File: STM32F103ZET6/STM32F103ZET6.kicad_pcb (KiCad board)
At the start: 2 copper layers, 1 part, among them U1 STM32F103ZETx

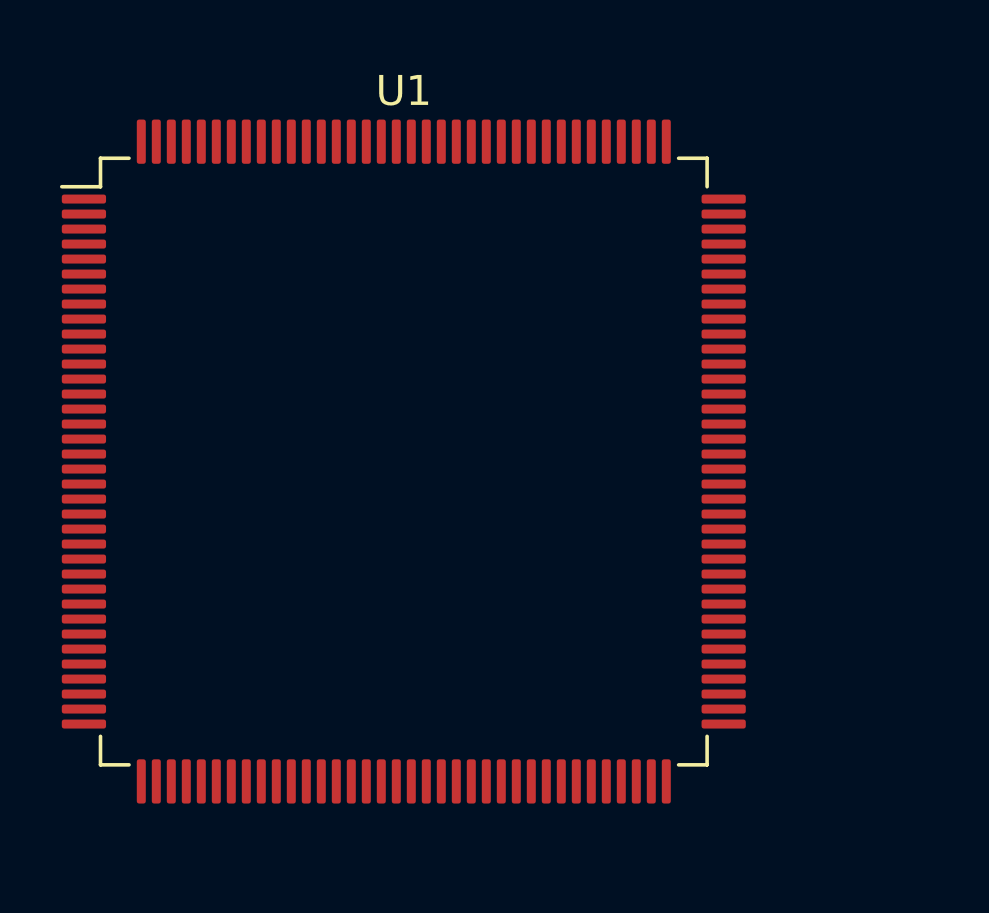
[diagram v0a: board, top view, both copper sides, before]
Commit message: add EEPROM & SPI Flash
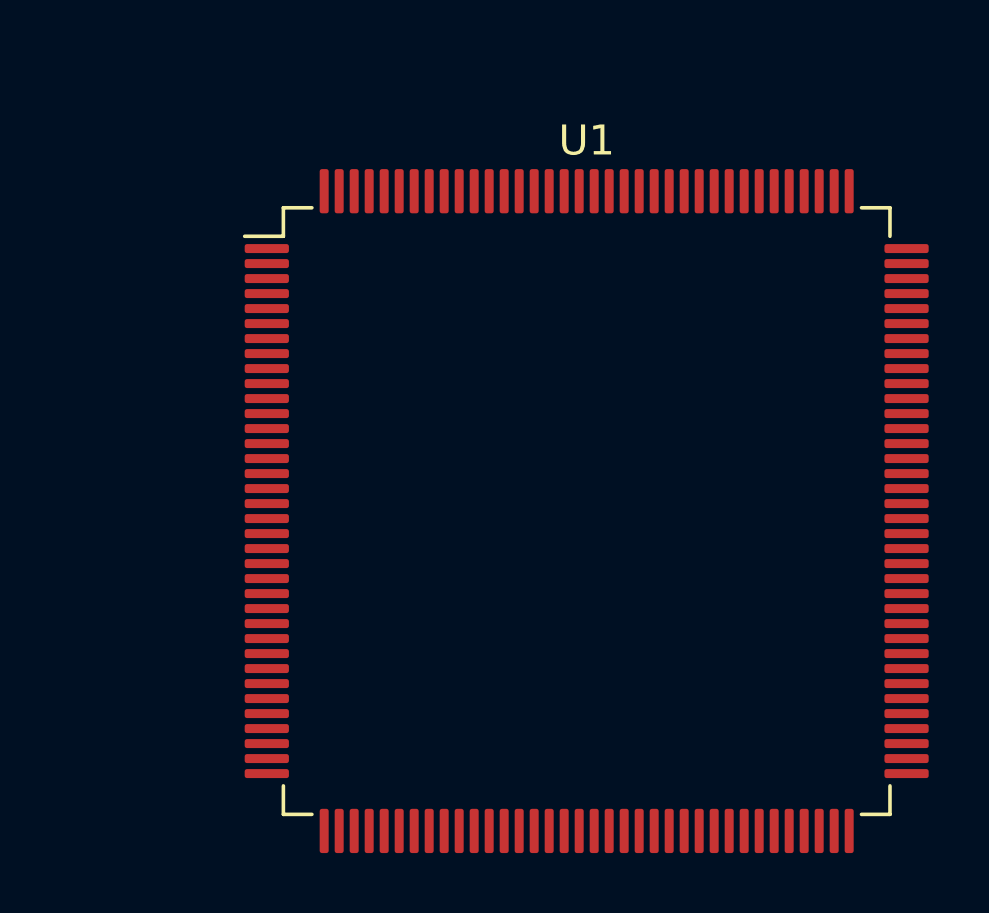
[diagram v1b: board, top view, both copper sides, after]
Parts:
- moved U1 6.32 mm to (152.1, 102.0)
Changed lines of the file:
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@@
     (solder_mask_min_width 0.25)
     (aux_axis_origin 0 0)
-    (visible_elements FFFFFF7F)
+    (grid_origin 152.4 101.727)
+    (visible_elements 7FFFFFFF)
     (pcbplotparams
       (layerselection 0x010fc_ffffffff)
@@
   )
   (module Package_QFP:LQFP-144_20x20mm_P0.5mm (layer F.Cu)
-    (at 146.05 100.33)
+    (at 152.146 101.981)
     (descr "LQFP, 144 Pin (http://ww1.microchip.com/downloads/en/PackagingSpec/00000049BQ.pdf#page=425), generated with kicad-footprint-generator ipc_gullwing_generator.py")
     (tags "LQFP QFP")
